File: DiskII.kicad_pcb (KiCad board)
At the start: 2 copper layers, 100 x 77.5 mm, 31 parts, among them J1 Apple II Expansion Bus, J2 DRIVE 2, J3 DRIVE 1, Q1 2N3906, Q2 MPSU51, Q3 MPSU51, SW1 A8, SW2 A9, SW3 A10

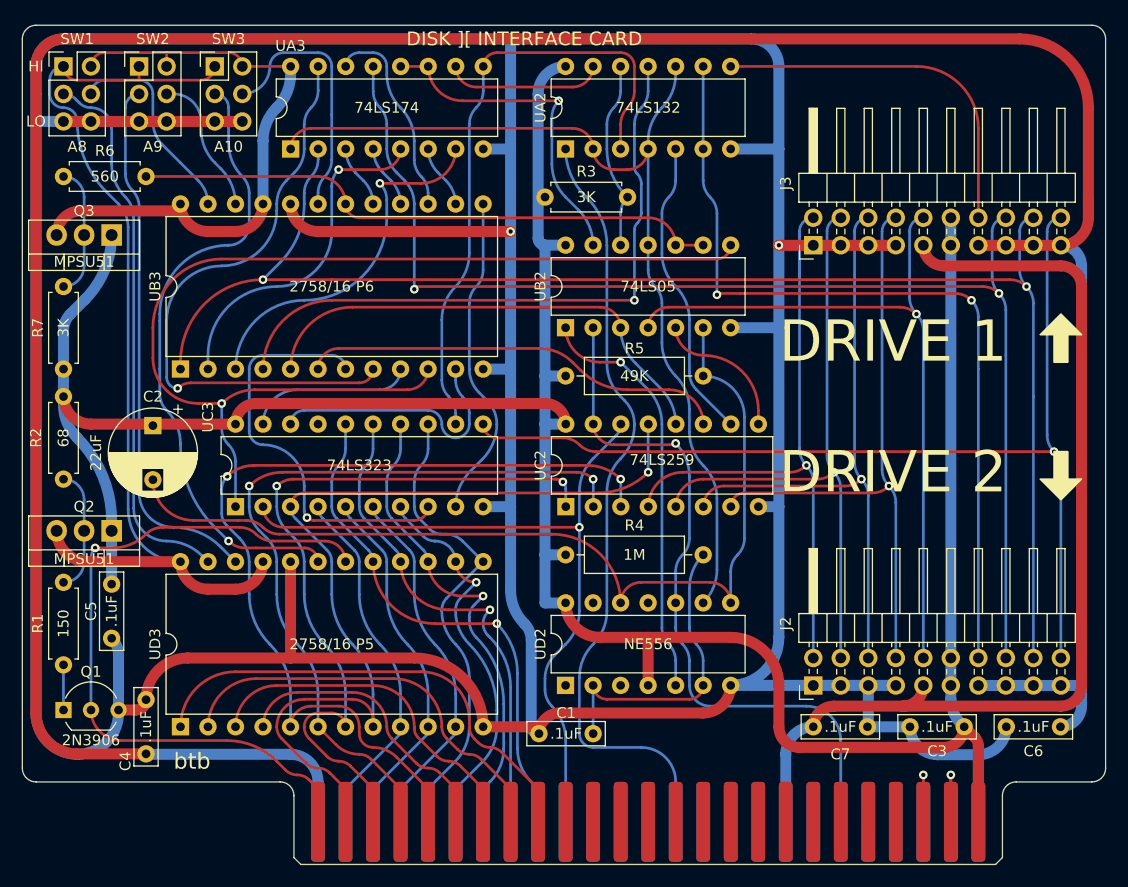
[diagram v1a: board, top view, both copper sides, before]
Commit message: fix misrouted data lines to shift register
a few other minor fixes
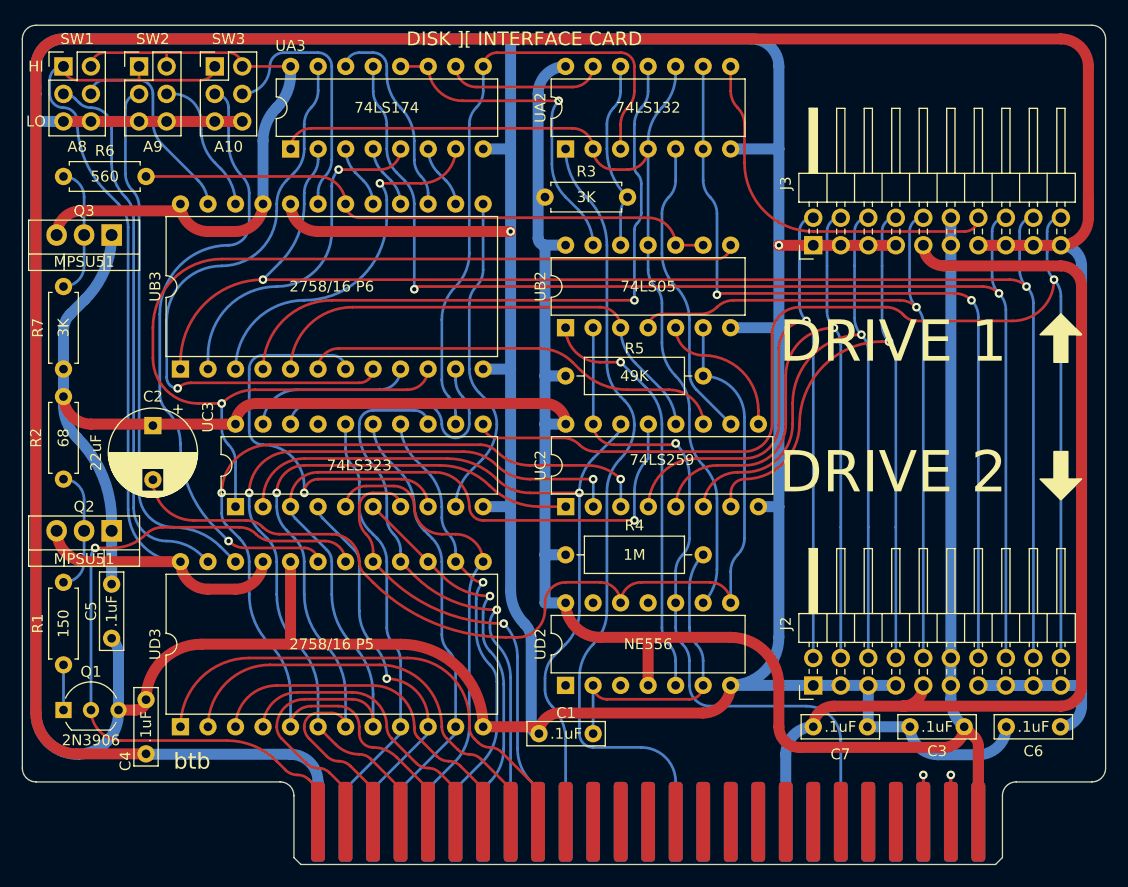
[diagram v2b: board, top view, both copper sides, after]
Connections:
- UC3 pad 13: /D3 -> /D6
- UC3 pad 14: /D5 -> /D4
- UC3 pad 15: /D6 -> /D2
- UC3 pad 16: /D7 -> /D0
- UC3 pad 4: /D0 -> /D1
- UC3 pad 5: /D1 -> /D3
- UC3 pad 6: /D2 -> /D5
- UC3 pad 7: /D4 -> /D7
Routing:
- net /W PROT: track 95.3 -> 108.6 mm
- net /PH0: track 63.7 -> 74.9 mm
- net /D5: track 43.9 -> 32.9 mm
- net /PH1: track 57.7 -> 67.1 mm
- net /PH2: track 57.4 -> 65.5 mm
- net /PH3: track 57.1 -> 64.9 mm
- net /D7: track 48.2 -> 41.2 mm
- net /D6: track 45.5 -> 51.8 mm
- net Net-(C2-Pad2): track 88.8 -> 93.1 mm
- net /D3: track 44.0 -> 40.0 mm
- net /D2: track 33.6 -> 37.3 mm
- net /A1: track 70.0 -> 66.3 mm, vias 2 -> 1
- net /A5: track 32.5 -> 29.4 mm
- net /A4: track 26.7 -> 23.7 mm
- net /A0: track 85.1 -> 88.1 mm
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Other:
- board text added: "To eliminate power-saving feature: DNP Q1 Q2 Q3 R1 R2 R6 R7 short Q2 pins 1 and 3 short Q3 pins 1 and 3"

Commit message: massive fixups
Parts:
- removed SW2: A9, Connector_PinHeader_2.54mm:PinHeader_2x03_P2.54mm_Vertical
- removed SW3: A10, Connector_PinHeader_2.54mm:PinHeader_2x03_P2.54mm_Vertical
- added JP5A10: A10, Jumper:SolderJumper-3_P1.3mm_Bridged12_RoundedPad1.0x1.5mm_NumberLabels, F.Cu at (135.3, 116.2)
- added JP5A9: A9, Jumper:SolderJumper-3_P1.3mm_Bridged12_RoundedPad1.0x1.5mm_NumberLabels, F.Cu at (130.2, 116.2)
- added JP6A10: A10, Jumper:SolderJumper-3_P1.3mm_Bridged12_RoundedPad1.0x1.5mm_NumberLabels, F.Cu at (135.3, 83.2)
- added JP6A9: A9, Jumper:SolderJumper-3_P1.3mm_Bridged12_RoundedPad1.0x1.5mm_NumberLabels, F.Cu at (130.2, 83.2)
- R1, R2, R3, R6, R7: footprint Resistor_THT:R_Axial_DIN0207_L6.3mm_D2.5mm_P7.62mm_Horizontal -> Resistor_THT:R_Axial_DIN0207_L6.3mm_D2.5mm_P10.16mm_Horizontal
- R4, R5: footprint Resistor_THT:R_Axial_DIN0309_L9.0mm_D3.2mm_P12.70mm_Horizontal -> Resistor_THT:R_Axial_DIN0207_L6.3mm_D2.5mm_P10.16mm_Horizontal
- UB3: value 2758/16 P6 -> 2758/16/32 P6
- UC2: value 74LS259 -> 74LS259/9334
- UD3: value 2758/16 P5 -> 2758/16/32 P5
- moved R6 33.5 mm to (125.7, 109.2), turned to 90 degrees
- moved C2 26.2 mm to (128.3, 74.8), turned to 90 degrees
- moved R4 24.3 mm to (179.1, 128.9), turned to 180 degrees
- moved R3 17.2 mm to (176.5, 80.0), turned to 180 degrees
- moved Q3 9.92 mm to (120.7, 92.7), turned to 90 degrees
- moved SWA8 8.05 mm to (117.5, 74.9)
- moved Q2 4.94 mm to (120.7, 105.4), turned to 90 degrees
- moved R5 2.54 mm to (176.5, 95.9)
- moved C4 2.50 mm to (122.6, 128.3)
- moved C5 2.40 mm to (120.7, 113.1)
- moved R1 1.91 mm to (114.9, 120.7)
- moved UA3 1.27 mm to (135.9, 76.2)
- moved UA2 1.27 mm to (161.3, 76.2)
- moved Q1 0.28 mm to (114.9, 127.0)
- renumbered SW1 to SWA8
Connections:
- net /P5A8 renamed Net-(SWA8-Pad2)
- net /P5VCC renamed Net-(JP5A10-Pad3)
- net /P6A0 renamed Net-(UA3-Pad15)
- net /P6A1 renamed Net-(UB3-Pad7)
- net /P6A2 renamed Net-(UB3-Pad6)
- net /P6A3 renamed Net-(UB2-Pad3)
- net /P6A4 renamed Net-(UA2-Pad11)
- net /P6A5 renamed Net-(UA3-Pad7)
- net /P6A6 renamed Net-(UA3-Pad5)
- net /P6A7 renamed /WR DATA
- net /P6A8 renamed Net-(SWA8-Pad5)
- net /P6D0 renamed Net-(UB3-Pad9)
- net /P6D1 renamed Net-(UB2-Pad8)
- net /P6D2 renamed Net-(UB3-Pad11)
- net /P6D3 renamed Net-(UB3-Pad13)
- net /P6D4 renamed Net-(UA3-Pad6)
- net /P6D5 renamed Net-(UA3-Pad14)
- net /P6D6 renamed Net-(UA3-Pad4)
- net /P6D7 renamed Net-(UA3-Pad3)
- net /P6EN renamed Net-(R6-Pad2)
- net /P6VCC renamed Net-(JP6A10-Pad3)
- UB3 pad 19: /P6A10 -> Net-(JP6A10-Pad2)
- UB3 pad 22: /P6A9 -> Net-(JP6A9-Pad2)
- UD3 pad 19: /P5A10 -> Net-(JP5A10-Pad2)
- UD3 pad 22: /P5A9 -> Net-(JP5A9-Pad2)
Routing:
- net /P5A10: track 57.7 -> 0.00 mm, vias 1 -> 0
- net /P5A9: track 49.4 -> 0.00 mm
- net Net-(JP5A10-Pad3): track 91.5 -> 58.2 mm
- net +5V: track 252.9 -> 281.5 mm
- net Net-(UA3-Pad15): track 55.6 -> 29.0 mm, vias 1 -> 0
- net Net-(UB2-Pad8): track 99.0 -> 75.0 mm, vias 1 -> 2
- net /P6A10: track 24.0 -> 0.00 mm
- net GND: track 458.9 -> 479.2 mm, vias 2 -> 1
- net Net-(C2-Pad2): track 93.1 -> 110.2 mm, vias 0 -> 1
- net Net-(Q3-Pad2): track 12.2 -> 28.8 mm
- net /P6A9: track 12.4 -> 0.00 mm
- net Net-(SWA8-Pad5): track 19.0 -> 9.60 mm
- net Net-(JP5A10-Pad2): track 0.00 -> 8.50 mm
- net Net-(JP6A10-Pad2): track 0.00 -> 8.49 mm
- net Net-(C1-Pad1): track 28.0 -> 20.4 mm
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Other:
- outline, holes or cut-outs redrawn
- board text added: "github.com/btb/DiskII"
- board text added: "rev ${REVISION}"
- board text removed: "HI"
- board text removed: "LO"
- board text removed: "btb"

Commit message: revision 1
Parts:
- added JP17: Unidisk, Jumper:SolderJumper-3_P1.3mm_Bridged12_RoundedPad1.0x1.5mm, B.Cu at (204.5, 78.1)
- added JP19: Unidisk, Jumper:SolderJumper-2_P1.3mm_Bridged_RoundedPad1.0x1.5mm, B.Cu at (207.0, 77.5)
- J1: value Apple II Expansion Bus -> Apple II Expansion Slot
- moved R4 22.5 mm to (163.8, 112.4), turned to 0 degrees
- moved Q2 12.7 mm to (120.7, 118.1)
- moved C5 12.7 mm to (120.7, 100.4)
- moved C4 7.62 mm to (114.9, 128.2)
- moved Q1 5.85 mm to (120.7, 128.3), turned to 90 degrees
- moved C2 3.40 mm to (125.9, 72.4), turned to 0 degrees
- moved C1 2.88 mm to (166.4, 130.2), turned to 0 degrees
- moved R3 2.62 mm to (174.0, 79.4)
- moved R5 2.54 mm to (174.0, 95.9)
- moved C7 2.50 mm to (181.7, 128.3)
- moved SWA8 1.41 mm to (118.1, 76.2)
- moved C3 1.27 mm to (196.8, 128.3)
- moved UA2 1.27 mm to (161.3, 74.9)
- moved UA3 1.27 mm to (135.9, 74.9)
- moved UC2 1.27 mm to (160.0, 108.0)
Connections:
- J3 pad 17: +12V -> Net-(J3-Pad17)
- J3 pad 19: +12V -> Net-(J3-Pad19)
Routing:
- net +5V: track 281.5 -> 370.4 mm
- net /RD DATA: track 122.2 -> 184.8 mm, vias 2 -> 0
- net GND: track 479.2 -> 538.3 mm, vias 1 -> 2
- net Net-(UB3-Pad7): track 37.1 -> 88.4 mm, vias 1 -> 0
- net /D4: track 38.4 -> 89.3 mm, vias 1 -> 0
- net /D6: track 51.8 -> 94.6 mm, vias 1 -> 0
- net /~{ENBL 2}: track 80.2 -> 121.1 mm, vias 2 -> 0
- net /WR DATA: track 143.8 -> 178.1 mm, vias 1 -> 0
- net Net-(UA3-Pad11): track 30.6 -> 63.5 mm, vias 1 -> 0
- net Net-(UA2-Pad11): track 58.3 -> 77.7 mm, vias 1 -> 0
- net /WR REQ: track 67.9 -> 86.9 mm, vias 1 -> 0
- net Net-(UA3-Pad5): track 31.6 -> 49.6 mm, vias 1 -> 0
- net +12V: track 273.5 -> 289.6 mm, vias 0 -> 2
- net Net-(UB2-Pad8): track 75.0 -> 88.7 mm, vias 2 -> 0
- net /A3: track 82.0 -> 69.0 mm
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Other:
- outline, holes or cut-outs redrawn
- board text added: "DISK ][ INTERFACE"
- board text removed: "DISK ][ INTERFACE CARD"
- board text removed: "To eliminate power-saving feature: DNP Q1 Q2 Q3 R1 R2 R6 R7 short Q2 pins 1 and 3 short Q3 pins 1 and 3"
